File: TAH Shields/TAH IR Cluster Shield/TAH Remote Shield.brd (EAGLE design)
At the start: 36 x 29.8 mm, 15 parts, among them T1 2N3904

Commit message: TAH Shields new version update
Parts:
- removed U$3: (no value), TAH:TAHLOGO
- R1, R2, R3, R4, R5: value (none) -> 1k
- moved U$1 11.4 mm to (18.2, 19.7), flipped to the bottom
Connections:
- net D3: no longer R5.1
- net D9: now also R5.1
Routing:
- net D9: track 0.00 -> 19.9 mm
- net D3: track 6.19 -> 0.00 mm
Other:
- board text added: "http://www.tah.io/start"
- board text removed: "by Revealing Hour Creations"
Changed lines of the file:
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@@
 <?xml version="1.0" encoding="utf-8"?>
 <!DOCTYPE eagle SYSTEM "eagle.dtd">
-<eagle version="6.4">
+<eagle version="7.0.0">
 <drawing>
 <settings>
@@
 <grid distance="0.1" unitdist="mm" unit="mm" style="lines" multiple="1" display="yes" altdistance="0.1" altunitdist="mm" altunit="mm"/>
 <layers>
-<layer number="1" name="Top" color="4" fill="1" visible="yes" active="yes"/>
+<layer number="1" name="Top" color="4" fill="1" visible="no" active="yes"/>
 <layer number="16" name="Bottom" color="1" fill="1" visible="yes" active="yes"/>
 <layer number="17" name="Pads" color="2" fill="1" visible="yes" active="yes"/>
@@
 <layer number="123" name="tTestmark" color="7" fill="1" visible="no" active="yes"/>
 <layer number="124" name="bTestmark" color="7" fill="1" visible="no" active="yes"/>
-<layer number="125" name="_tNames" color="7" fill="1" visible="yes" active="yes"/>
-<layer number="126" name="_bNames" color="7" fill="1" visible="yes" active="yes"/>
+<layer number="125" name="_tNames" color="7" fill="1" visible="no" active="yes"/>
+<layer number="126" name="_bNames" color="7" fill="1" visible="no" active="yes"/>
 <layer number="127" name="_tValues" color="7" fill="1" visible="no" active="yes"/>
 <layer number="128" name="_bValues" color="7" fill="1" visible="no" active="yes"/>
@@
 <text x="29.9" y="2" size="1.016" layer="125" font="vector" align="center">L3</text>
 <text x="6.5" y="2.1" size="1.016" layer="125" font="vector" align="center">L4</text>
-<text x="18.2" y="15.6" size="1.016" layer="22" font="vector" ratio="26" rot="MR180" align="center">Made In India
-</text>
-<text x="18.2" y="14.1" size="0.8128" layer="22" font="vector" ratio="26" rot="MR180" align="center">by Revealing Hour Creations
-</text>
 <text x="14.3" y="0.8" size="1.016" layer="125">R2</text>
 <text x="20.4" y="0.8" size="1.016" layer="125" rot="SR0">R1</text>
@@
 <text x="15.1" y="18" size="1.016" layer="125">R3</text>
 <text x="19.5" y="18" size="1.016" layer="125">R4</text>
+<text x="18.2" y="14.7" size="1.016" layer="22" rot="MR0" align="center">http://www.tah.io/start</text>
+<text x="18.2" y="16.3" size="1.016" layer="22" rot="MR0" align="center">Made In India</text>
 </plain>
 <attributes>
@@
 <pass name="Default">
 <param name="RoutingGrid" value="0.1mm"/>
+<param name="AutoGrid" value="1"/>
+<param name="Efforts" value="0"/>
+<param name="TopRouterVariant" value="1"/>
 <param name="tpViaShape" value="octagon"/>
 <param name="PrefDir.1" value="|"/>
@@
 <element name="LED3" library="1n4148 diode sot 23" package="LED5MM" value="" x="9.4" y="21" rot="R225"/>
 <element name="LED4" library="1n4148 diode sot 23" package="LED5MM" value="" x="26.5" y="21" rot="R315"/>
-<element name="R1" library="1n4148 diode sot 23" package="M1206" value="" x="21.1" y="4.2" rot="R270"/>
-<element name="R2" library="1n4148 diode sot 23" package="M1206" value="" x="15.1" y="4.2" rot="R270"/>
-<element name="R3" library="1n4148 diode sot 23" package="M1206" value="" x="15.9" y="21.5" rot="R90"/>
-<element name="R4" library="1n4148 diode sot 23" package="M1206" value="" x="20.3" y="21.5" rot="R90"/>
-<element name="R5" library="1n4148 diode sot 23" package="M1206" value="" x="27.6" y="11.7" rot="R180"/>
+<element name="R1" library="1n4148 diode sot 23" package="M1206" value="1k" x="21.1" y="4.2" rot="R270"/>
+<element name="R2" library="1n4148 diode sot 23" package="M1206" value="1k" x="15.1" y="4.2" rot="R270"/>
+<element name="R3" library="1n4148 diode sot 23" package="M1206" value="1k" x="15.9" y="21.5" rot="R90"/>
+<element name="R4" library="1n4148 diode sot 23" package="M1206" value="1k" x="20.3" y="21.5" rot="R90"/>
+<element name="R5" library="1n4148 diode sot 23" package="M1206" value="1k" x="27.6" y="11.7" rot="R180"/>
 <element name="RC1" library="Infrared Receiver TSOP" package="PNA460XM" value="PNA460XM" x="18.1" y="13.5" rot="R180"/>
-<element name="U$1" library="TAH" package="TAHLOGO" value="" x="8.8" y="13.2"/>
 <element name="U$4" library="TAH" package="TAH_PIN_FOOTPRINT_WITHOUT_ICSP_VERS1.0_SILK" value="" x="18.2" y="14.3"/>
-<element name="U$3" library="TAH" package="TAHLOGO" value="" x="18.2" y="21.6" rot="MR0"/>
+<element name="U$1" library="TAH" package="TAHLOGO" value="" x="18.2" y="19.7" rot="MR0"/>
 </elements>
 <signals>
@@
 </signal>
 <signal name="D3">
-<contactref element="R5" pad="1"/>
 <contactref element="U$2" pad="D3"/>
-<wire x1="31.6" y1="11.7" x2="29" y2="11.7" width="0.254" layer="1"/>
-<wire x1="33.1" y1="13.1" x2="31.6" y2="11.7" width="0.254" layer="1"/>
-<wire x1="34.6" y1="13.1" x2="33.1" y2="13.1" width="0.254" layer="1"/>
-<wire x1="34.6" y1="13.1" x2="34.61" y2="13.14" width="0.254" layer="1"/>
 </signal>
 <signal name="5V">
@@
 <signal name="D9">
 <contactref element="U$2" pad="D9"/>
+<contactref element="R5" pad="1"/>
+<wire x1="29" y1="11.7" x2="30.3" y2="11.7" width="0.3048" layer="1"/>
+<wire x1="30.3" y1="11.7" x2="30.9" y2="12.3" width="0.3048" layer="1"/>
+<wire x1="30.9" y1="12.3" x2="30.9" y2="20.8" width="0.3048" layer="1"/>
+<wire x1="30.9" y1="20.8" x2="27" y2="24.7" width="0.3048" layer="1"/>
+<wire x1="27" y1="24.7" x2="27" y2="28.45" width="0.3048" layer="1"/>
+<wire x1="27" y1="28.45" x2="26.99" y2="28.46" width="0.3048" layer="1"/>
 </signal>
 <signal name="D10">
@@
 </board>
 </drawing>
-<compatibility>
-<note version="6.3" minversion="6.2.2" severity="warning">
-Since Version 6.2.2 text objects can contain more than one line,
-which will not be processed correctly with this version.
-</note>
-</compatibility>
 </eagle>

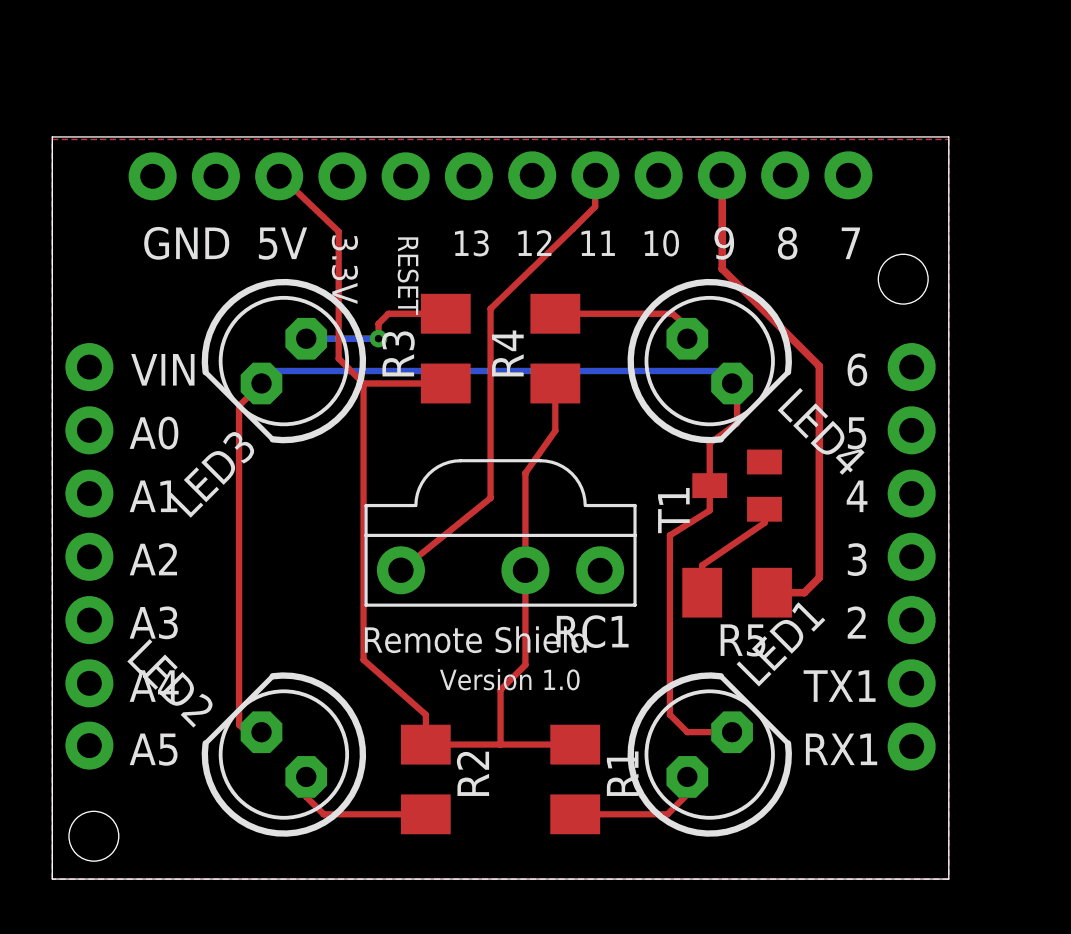
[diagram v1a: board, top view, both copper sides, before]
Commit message: All shields updated with latest Tah footprint
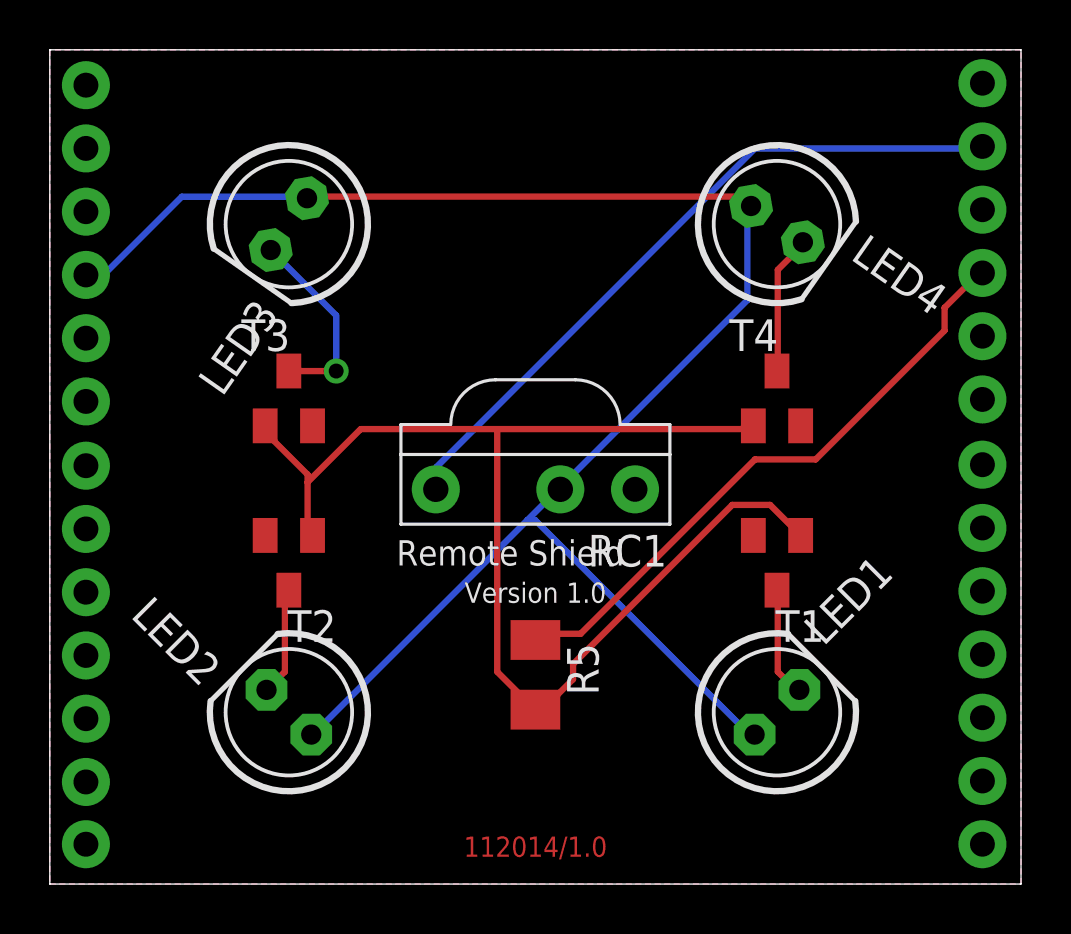
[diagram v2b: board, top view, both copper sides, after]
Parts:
- removed R1, R2, R3, R4: 1k, 1n4148 diode sot 23:M1206
- added T2, T3, T4: 2N3904, semicon-smd-ipc:SOT23
- moved U$2 12.1 mm to (19.0, 15.0)
- moved R5 8.75 mm to (19.5, 8.40), turned to 270 degrees
- moved U$1 7.69 mm to (19.4, 12.1)
- moved LED4 6.13 mm to (29.2, 26.5), turned to 325 degrees
- moved LED3 5.50 mm to (9.60, 26.5), turned to 235 degrees
- moved RC1 3.54 mm to (19.5, 16.8)
- moved T1 3.49 mm to (29.2, 12.9), turned to 180 degrees
- moved LED1 3.19 mm to (29.2, 6.90)
- moved U$4 2.73 mm to (19.5, 16.7)
- moved LED2 1.71 mm to (9.60, 6.90)
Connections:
- removed net N$6: R5.2, T1.1
- net 5V: now also LED1.A, LED2.A, LED3.A, LED4.A; no longer R1.1, R2.1, R3.1, R4.1
- net GND: now also T2.2, T3.2, T4.2
- net N$1: now also LED1.K, T1.3; no longer LED1.A, R1.2
- net N$2: now also LED2.K, T2.3; no longer LED2.A, R2.2
- net N$3: now also LED4.K, T4.3; no longer LED3.A, R3.2
- net N$4: now also LED3.K, T3.3; no longer LED4.A, R4.2
- net N$5: now also R5.2, T1.1, T2.1, T3.1, T4.1; no longer LED1.K, LED2.K, LED3.K, LED4.K, T1.3
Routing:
- net 5V: track 50.0 -> 69.5 mm
- net D11: track 19.4 -> 28.1 mm
- net N$6: track 4.67 -> 0.00 mm
- net D9: track 19.9 -> 24.6 mm
- net N$4: track 5.98 -> 7.85 mm, vias 0 -> 1
- net N$2: track 5.89 -> 4.36 mm
- net N$1: track 5.53 -> 4.42 mm
- net N$5: track 52.0 -> 51.0 mm
- net N$3: track 6.37 -> 5.58 mm, vias 1 -> 0
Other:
- board size 36 x 29.8 mm -> 39 x 33.5 mm
- board text added: "112014/1.0"
- board text added: "http://tah.io/start"
- board text removed: "L1"
- board text removed: "L2"
- board text removed: "L3"
- board text removed: "L4"
- board text removed: "R1"
- board text removed: "R2"
- board text removed: "R3"
- board text removed: "R4"
- board text removed: "R5"
- board text removed: "T1"
- board text removed: "http://www.tah.io/start"

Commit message: Updated production ready files for Tah and shields
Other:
- board text added: "122014/1.0"
- board text removed: "112014/1.0"
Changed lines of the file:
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@@
 <text x="19.4" y="7.1" size="1.016" layer="22" rot="MR0" align="center">http://tah.io/start</text>
 <text x="19.4" y="8.7" size="1.016" layer="22" rot="MR0" align="center">Made In India</text>
-<text x="19.5" y="1.5" size="0.8128" layer="1" align="center">112014/1.0</text>
+<text x="19.5" y="1.5" size="0.8128" layer="1" align="center">122014/1.0</text>
 </plain>
 <attributes>
